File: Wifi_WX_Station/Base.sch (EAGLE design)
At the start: 75 parts, among them IC1 3.3v, J1 RJ45-8VERT, J6 M05X22X5FE, Q1 32.768Khz, U1 CP2104-GM, U2 25LC512, U3 PIC24FJ128GA008

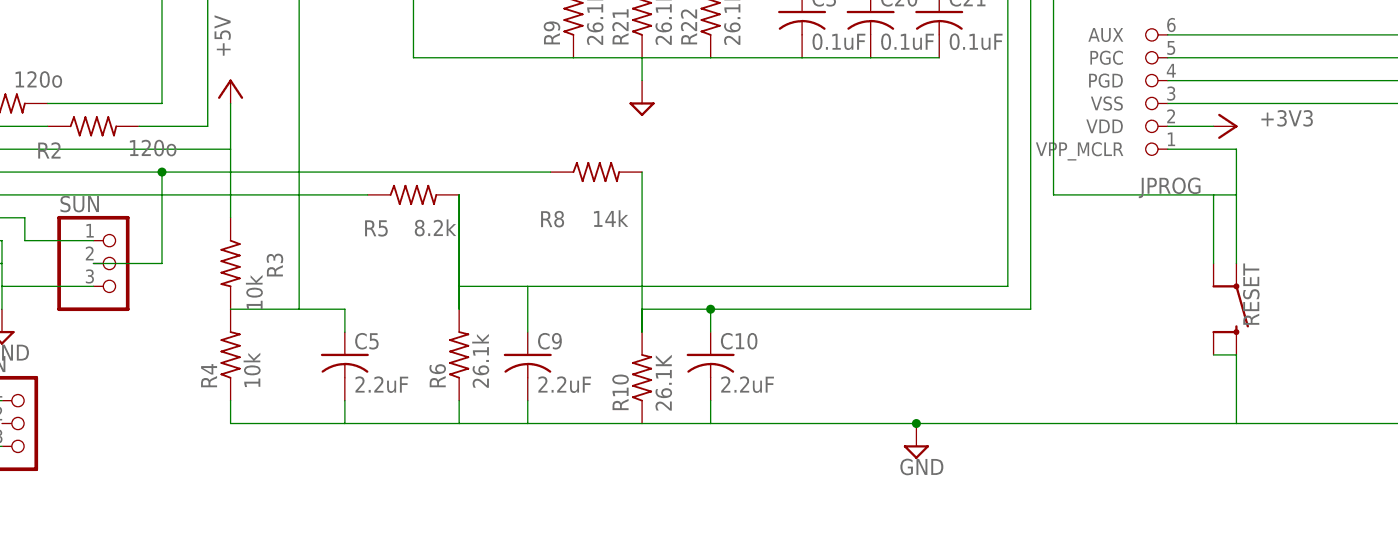
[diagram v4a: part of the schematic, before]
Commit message: 
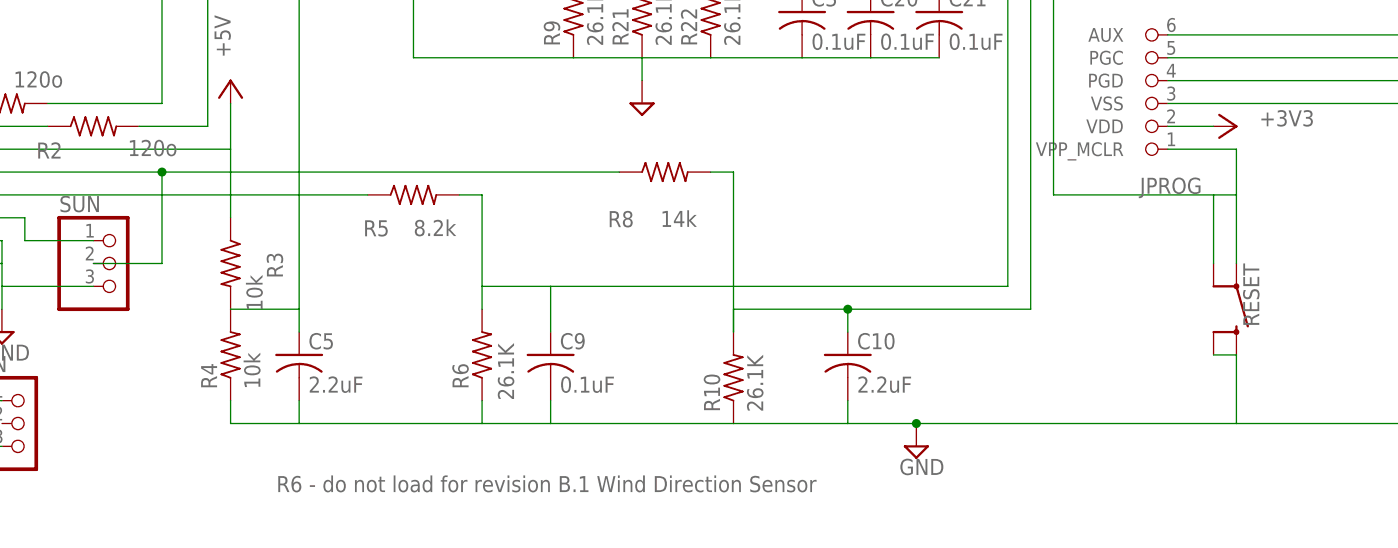
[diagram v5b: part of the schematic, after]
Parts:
- C9: value 2.2uF -> 0.1uF
- R6: value 26.1k -> 26.1K
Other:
- note added: "R6 - do not load for revision B.1 Wind Direction Sensor"
- moved on the sheet: C10, C5, C9, R10, R6, R8
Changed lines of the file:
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@@
 <part name="P+1" library="supply1" deviceset="+5V" device=""/>
 <part name="R5" library="rcl" deviceset="R-US_" device="R0603" value="8.2k"/>
-<part name="R6" library="rcl" deviceset="R-US_" device="R0603" value="26.1k"/>
-<part name="C9" library="rcl" deviceset="C-US" device="C0805" value="2.2uF"/>
+<part name="R6" library="rcl" deviceset="R-US_" device="R0603" value="26.1K"/>
+<part name="C9" library="rcl" deviceset="C-US" device="C0805" value="0.1uF"/>
 <part name="R13" library="rcl" deviceset="R-US_" device="R0603" value="2.2K"/>
 <part name="R3" library="rcl" deviceset="R-US_" device="R0603" value="10k"/>
@@
 <text x="-83.82" y="55.88" size="1.27" layer="95">PIC24FJ256GA108</text>
 <text x="43.18" y="78.74" size="1.778" layer="95">MRF24</text>
+<text x="-226.06" y="-40.64" size="1.778" layer="96">R6 - do not load for revision B.1 Wind Direction Sensor</text>
 </plain>
 <instances>
@@
 <attribute name="VALUE" x="-210.82" y="-12.192" size="1.778" layer="96"/>
 </instance>
-<instance part="R6" gate="G$1" x="-205.74" y="-25.4" rot="R90"/>
-<instance part="C9" gate="G$1" x="-198.12" y="-25.4"/>
+<instance part="R6" gate="G$1" x="-203.2" y="-25.4" smashed="yes" rot="R90">
+<attribute name="NAME" x="-204.6986" y="-29.21" size="1.778" layer="95" rot="R90"/>
+<attribute name="VALUE" x="-201.422" y="-24.13" size="1.778" layer="96" rot="R270"/>
+</instance>
+<instance part="C9" gate="G$1" x="-195.58" y="-25.4"/>
 <instance part="R13" gate="G$1" x="-157.48" y="106.68" smashed="yes" rot="R90">
 <attribute name="NAME" x="-158.9786" y="100.33" size="1.778" layer="95" rot="R90"/>
@@
 <attribute name="VALUE" x="-229.362" y="-16.51" size="1.778" layer="96" rot="R270"/>
 </instance>
-<instance part="C10" gate="G$1" x="-177.8" y="-25.4"/>
-<instance part="R8" gate="G$1" x="-190.5" y="-5.08" smashed="yes">
-<attribute name="NAME" x="-196.85" y="-11.2014" size="1.778" layer="95"/>
-<attribute name="VALUE" x="-191.008" y="-11.176" size="1.778" layer="96"/>
-</instance>
-<instance part="R10" gate="G$1" x="-185.42" y="-27.94" rot="R90"/>
+<instance part="C10" gate="G$1" x="-162.56" y="-25.4"/>
+<instance part="R8" gate="G$1" x="-182.88" y="-5.08" smashed="yes">
+<attribute name="NAME" x="-189.23" y="-11.2014" size="1.778" layer="95"/>
+<attribute name="VALUE" x="-183.388" y="-11.176" size="1.778" layer="96"/>
+</instance>
+<instance part="R10" gate="G$1" x="-175.26" y="-27.94" rot="R90"/>
 <instance part="R4" gate="G$1" x="-231.14" y="-25.4" rot="R90"/>
 <instance part="R15" gate="G$1" x="-152.4" y="106.68" smashed="yes" rot="R90">
@@
 <instance part="C16" gate="G$1" x="-187.96" y="111.76"/>
 <instance part="C18" gate="G$1" x="-175.26" y="111.76"/>
-<instance part="C5" gate="G$1" x="-218.44" y="-25.4"/>
+<instance part="C5" gate="G$1" x="-223.52" y="-25.4"/>
 <instance part="SUPPLY11" gate="GND" x="-264.16" y="-40.64"/>
 <instance part="P+3" gate="1" x="-264.16" y="-25.4" smashed="yes">
@@
 <pinref part="C9" gate="G$1" pin="2"/>
 <pinref part="R6" gate="G$1" pin="1"/>
-<wire x1="-205.74" y1="-30.48" x2="-205.74" y2="-33.02" width="0.1524" layer="91"/>
+<wire x1="-203.2" y1="-30.48" x2="-203.2" y2="-33.02" width="0.1524" layer="91"/>
 <pinref part="C10" gate="G$1" pin="2"/>
-<wire x1="-198.12" y1="-33.02" x2="-205.74" y2="-33.02" width="0.1524" layer="91"/>
-<wire x1="-198.12" y1="-30.48" x2="-198.12" y2="-33.02" width="0.1524" layer="91"/>
-<wire x1="-198.12" y1="-33.02" x2="-185.42" y2="-33.02" width="0.1524" layer="91"/>
-<wire x1="-185.42" y1="-33.02" x2="-177.8" y2="-33.02" width="0.1524" layer="91"/>
-<wire x1="-177.8" y1="-33.02" x2="-177.8" y2="-30.48" width="0.1524" layer="91"/>
+<wire x1="-195.58" y1="-33.02" x2="-203.2" y2="-33.02" width="0.1524" layer="91"/>
+<wire x1="-195.58" y1="-30.48" x2="-195.58" y2="-33.02" width="0.1524" layer="91"/>
+<wire x1="-195.58" y1="-33.02" x2="-175.26" y2="-33.02" width="0.1524" layer="91"/>
+<wire x1="-175.26" y1="-33.02" x2="-162.56" y2="-33.02" width="0.1524" layer="91"/>
+<wire x1="-162.56" y1="-33.02" x2="-162.56" y2="-30.48" width="0.1524" layer="91"/>
 <pinref part="R10" gate="G$1" pin="1"/>
 <pinref part="R4" gate="G$1" pin="1"/>
-<wire x1="-177.8" y1="-33.02" x2="-119.38" y2="-33.02" width="0.1524" layer="91"/>
+<wire x1="-162.56" y1="-33.02" x2="-119.38" y2="-33.02" width="0.1524" layer="91"/>
 <wire x1="-119.38" y1="-33.02" x2="-83.82" y2="-33.02" width="0.1524" layer="91"/>
 <wire x1="-231.14" y1="-30.48" x2="-231.14" y2="-33.02" width="0.1524" layer="91"/>
-<wire x1="-231.14" y1="-33.02" x2="-218.44" y2="-33.02" width="0.1524" layer="91"/>
+<wire x1="-231.14" y1="-33.02" x2="-223.52" y2="-33.02" width="0.1524" layer="91"/>
 <pinref part="C5" gate="G$1" pin="2"/>
-<wire x1="-218.44" y1="-33.02" x2="-205.74" y2="-33.02" width="0.1524" layer="91"/>
-<wire x1="-218.44" y1="-30.48" x2="-218.44" y2="-33.02" width="0.1524" layer="91"/>
+<wire x1="-223.52" y1="-33.02" x2="-203.2" y2="-33.02" width="0.1524" layer="91"/>
+<wire x1="-223.52" y1="-30.48" x2="-223.52" y2="-33.02" width="0.1524" layer="91"/>
 <pinref part="SV1" gate="G$1" pin="1"/>
 <pinref part="RESET" gate="G$1" pin="2"/>
@@
 <net name="WIND_ADC_IN" class="0">
 <segment>
-<wire x1="-144.78" y1="-17.78" x2="-198.12" y2="-17.78" width="0.1524" layer="91"/>
-<wire x1="-205.74" y1="-17.78" x2="-205.74" y2="-7.62" width="0.1524" layer="91"/>
+<wire x1="-144.78" y1="-17.78" x2="-195.58" y2="-17.78" width="0.1524" layer="91"/>
+<wire x1="-203.2" y1="-17.78" x2="-203.2" y2="-7.62" width="0.1524" layer="91"/>
+<wire x1="-203.2" y1="-7.62" x2="-205.74" y2="-7.62" width="0.1524" layer="91"/>
 <pinref part="R6" gate="G$1" pin="2"/>
 <pinref part="C9" gate="G$1" pin="1"/>
-<wire x1="-205.74" y1="-20.32" x2="-205.74" y2="-17.78" width="0.1524" layer="91"/>
-<wire x1="-205.74" y1="-17.78" x2="-198.12" y2="-17.78" width="0.1524" layer="91"/>
-<wire x1="-198.12" y1="-17.78" x2="-198.12" y2="-22.86" width="0.1524" layer="91"/>
+<wire x1="-203.2" y1="-20.32" x2="-203.2" y2="-17.78" width="0.1524" layer="91"/>
+<wire x1="-203.2" y1="-17.78" x2="-195.58" y2="-17.78" width="0.1524" layer="91"/>
+<wire x1="-195.58" y1="-17.78" x2="-195.58" y2="-22.86" width="0.1524" layer="91"/>
 <pinref part="R5" gate="G$1" pin="2"/>
 <pinref part="U3" gate="G$1" pin="C1IN-/AN4/CN6/RB4"/>
 <wire x1="-144.78" y1="-17.78" x2="-144.78" y2="35.56" width="0.1524" layer="91"/>
 <wire x1="-144.78" y1="35.56" x2="-134.62" y2="35.56" width="0.1524" layer="91"/>
-<wire x1="-205.74" y1="-7.62" x2="-205.74" y2="-20.32" width="0.1524" layer="91"/>
 </segment>
 </net>
@@
 <segment>
 <wire x1="-142.24" y1="33.02" x2="-142.24" y2="-20.32" width="0.1524" layer="91"/>
-<wire x1="-142.24" y1="-20.32" x2="-177.8" y2="-20.32" width="0.1524" layer="91"/>
+<wire x1="-142.24" y1="-20.32" x2="-162.56" y2="-20.32" width="0.1524" layer="91"/>
 <pinref part="R8" gate="G$1" pin="2"/>
 <pinref part="R10" gate="G$1" pin="2"/>
-<wire x1="-177.8" y1="-20.32" x2="-185.42" y2="-20.32" width="0.1524" layer="91"/>
-<wire x1="-185.42" y1="-20.32" x2="-185.42" y2="-22.86" width="0.1524" layer="91"/>
-<wire x1="-185.42" y1="-22.86" x2="-185.42" y2="-5.08" width="0.1524" layer="91"/>
+<wire x1="-162.56" y1="-20.32" x2="-175.26" y2="-20.32" width="0.1524" layer="91"/>
+<wire x1="-175.26" y1="-20.32" x2="-175.26" y2="-22.86" width="0.1524" layer="91"/>
+<wire x1="-175.26" y1="-22.86" x2="-175.26" y2="-5.08" width="0.1524" layer="91"/>
+<wire x1="-175.26" y1="-5.08" x2="-177.8" y2="-5.08" width="0.1524" layer="91"/>
 <pinref part="U3" gate="G$1" pin="C2IN+/AN3/CN5/RB3"/>
 <wire x1="-142.24" y1="33.02" x2="-134.62" y2="33.02" width="0.1524" layer="91"/>
 <pinref part="C10" gate="G$1" pin="1"/>
-<wire x1="-177.8" y1="-22.86" x2="-177.8" y2="-20.32" width="0.1524" layer="91"/>
-<junction x="-177.8" y="-20.32"/>
+<wire x1="-162.56" y1="-22.86" x2="-162.56" y2="-20.32" width="0.1524" layer="91"/>
+<junction x="-162.56" y="-20.32"/>
 </segment>
 </net>
@@
 <segment>
 <pinref part="R8" gate="G$1" pin="1"/>
-<wire x1="-195.58" y1="-5.08" x2="-238.76" y2="-5.08" width="0.1524" layer="91"/>
+<wire x1="-187.96" y1="-5.08" x2="-238.76" y2="-5.08" width="0.1524" layer="91"/>
 <label x="-281.94" y="-5.08" size="0.8128" layer="95" rot="R180" xref="yes"/>
 <wire x1="-238.76" y1="-5.08" x2="-264.16" y2="-5.08" width="0.1524" layer="91"/>
@@
 <segment>
 <wire x1="-223.52" y1="38.1" x2="-134.62" y2="38.1" width="0.1524" layer="91"/>
-<wire x1="-218.44" y1="-20.32" x2="-223.52" y2="-20.32" width="0.1524" layer="91"/>
 <wire x1="-223.52" y1="-20.32" x2="-223.52" y2="38.1" width="0.1524" layer="91"/>
 <pinref part="U3" gate="G$1" pin="C1IN+/AN5/CN7/RB5"/>
@@
 <pinref part="R3" gate="G$1" pin="2"/>
 <pinref part="C5" gate="G$1" pin="1"/>
-<wire x1="-218.44" y1="-22.86" x2="-218.44" y2="-20.32" width="0.1524" layer="91"/>
+<wire x1="-223.52" y1="-22.86" x2="-223.52" y2="-20.32" width="0.1524" layer="91"/>
 <wire x1="-223.52" y1="-20.32" x2="-231.14" y2="-20.32" width="0.1524" layer="91"/>
 </segment>

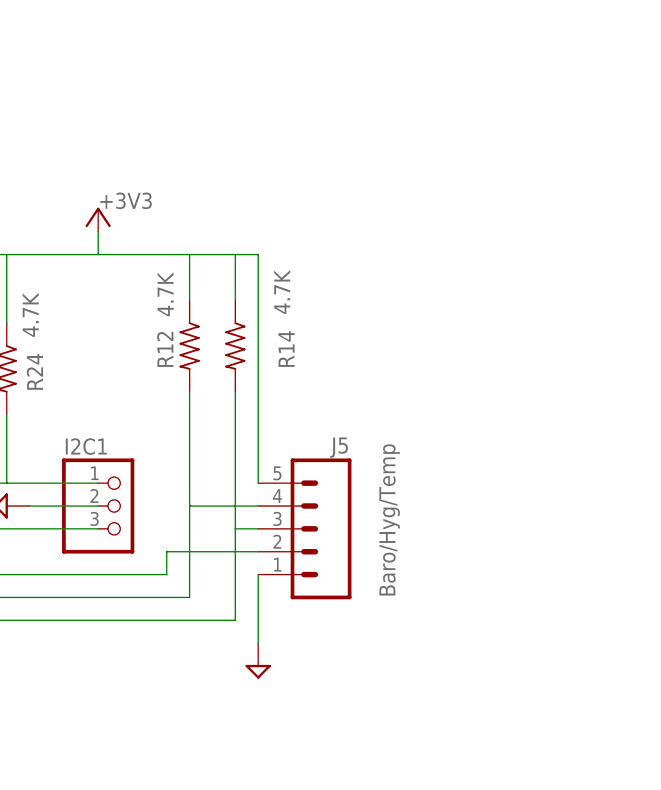
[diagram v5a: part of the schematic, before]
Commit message: Changed to RJ11 connector for Baro_temp_hyg  on base board -- Cleaned up some silk screen stuff Added new RJ11 based Baro_Temp_Hyg board layout
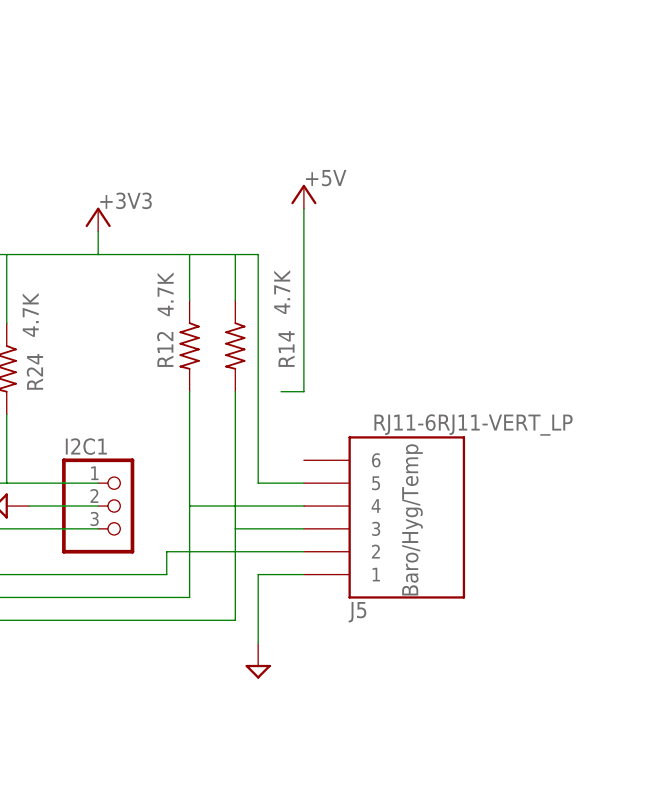
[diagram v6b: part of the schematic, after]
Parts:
- J5: value (none) -> RJ11-6RJ11-VERT_LP; device wifi_WX:M05MOLEX_KK -> wifi_WX:RJ11-6RJ11-VERT_LP
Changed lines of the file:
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@@
 <part name="C20" library="rcl" deviceset="C-US" device="C0805" value="0.1uF"/>
 <part name="C21" library="rcl" deviceset="C-US" device="C0805" value="0.1uF"/>
-<part name="J5" library="wifi_WX" deviceset="M05" device="MOLEX_KK"/>
 <part name="SUPPLY13" library="supply2" deviceset="GND" device=""/>
 <part name="R23" library="rcl" deviceset="R-US_" device="R0603" value="4.7K"/>
@@
 <part name="P+4" library="supply1" deviceset="+5V" device=""/>
 <part name="D2" library="diode" deviceset="MBR0520LT" device=""/>
+<part name="P+5" library="supply1" deviceset="+5V" device=""/>
+<part name="J5" library="wifi_WX" deviceset="RJ11-6" device="RJ11-VERT_LP"/>
 </parts>
 <sheets>
 <sheet>
 <plain>
-<text x="124.46" y="40.64" size="1.778" layer="95" rot="R90">Baro/Hyg/Temp</text>
+<text x="127" y="40.64" size="1.778" layer="95" rot="R90">Baro/Hyg/Temp</text>
 <text x="-83.82" y="55.88" size="1.27" layer="95">PIC24FJ256GA108</text>
 <text x="43.18" y="78.74" size="1.778" layer="95">MRF24</text>
@@
 <instance part="C20" gate="G$1" x="-160.02" y="12.7"/>
 <instance part="C21" gate="G$1" x="-152.4" y="12.7"/>
-<instance part="J5" gate="G$1" x="116.84" y="48.26" rot="MR0"/>
 <instance part="SUPPLY13" gate="GND" x="81.28" y="50.8" smashed="yes" rot="R270"/>
 <instance part="R23" gate="G$1" x="76.2" y="66.04" smashed="yes" rot="R270">
@@
 </instance>
 <instance part="D2" gate="G$1" x="-233.68" y="33.02" rot="R270"/>
+<instance part="P+5" gate="1" x="114.3" y="86.36" smashed="yes">
+<attribute name="VALUE" x="114.3" y="86.36" size="1.778" layer="96"/>
+</instance>
+<instance part="J5" gate="G$1" x="124.46" y="53.34" rot="MR180"/>
 </instances>
 <busses>
@@
 <segment>
 <pinref part="SUPPLY12" gate="GND" pin="GND"/>
+<wire x1="109.22" y1="43.18" x2="109.22" y2="35.56" width="0.1524" layer="91"/>
+<wire x1="109.22" y1="43.18" x2="114.3" y2="43.18" width="0.1524" layer="91"/>
 <pinref part="J5" gate="G$1" pin="1"/>
-<wire x1="109.22" y1="43.18" x2="109.22" y2="35.56" width="0.1524" layer="91"/>
 </segment>
 <segment>
@@
 <wire x1="91.44" y1="78.74" x2="101.6" y2="78.74" width="0.1524" layer="91"/>
 <wire x1="106.68" y1="78.74" x2="101.6" y2="78.74" width="0.1524" layer="91"/>
-<pinref part="J5" gate="G$1" pin="5"/>
 <wire x1="109.22" y1="78.74" x2="109.22" y2="53.34" width="0.1524" layer="91"/>
 <wire x1="106.68" y1="78.74" x2="109.22" y2="78.74" width="0.1524" layer="91"/>
@@
 <wire x1="81.28" y1="78.74" x2="91.44" y2="78.74" width="0.1524" layer="91"/>
 <wire x1="81.28" y1="71.12" x2="81.28" y2="78.74" width="0.1524" layer="91"/>
+<wire x1="109.22" y1="53.34" x2="114.3" y2="53.34" width="0.1524" layer="91"/>
+<pinref part="J5" gate="G$1" pin="5"/>
 </segment>
 </net>
@@
 <wire x1="-12.7" y1="40.64" x2="101.6" y2="40.64" width="0.1524" layer="91"/>
 <wire x1="101.6" y1="40.64" x2="101.6" y2="50.8" width="0.1524" layer="91"/>
-<wire x1="101.6" y1="50.8" x2="109.22" y2="50.8" width="0.1524" layer="91"/>
+<wire x1="101.6" y1="50.8" x2="114.3" y2="50.8" width="0.1524" layer="91"/>
 <pinref part="U3" gate="G$1" pin="SCL1/RG2"/>
 <label x="71.12" y="40.64" size="1.27" layer="95" rot="R180" xref="yes"/>
@@
 <wire x1="-12.7" y1="38.1" x2="106.68" y2="38.1" width="0.1524" layer="91"/>
 <wire x1="106.68" y1="38.1" x2="106.68" y2="48.26" width="0.1524" layer="91"/>
-<wire x1="106.68" y1="48.26" x2="109.22" y2="48.26" width="0.1524" layer="91"/>
 <pinref part="U3" gate="G$1" pin="SDA1/RG3"/>
 <label x="71.12" y="38.1" size="1.27" layer="95" rot="R180" xref="yes"/>
 <pinref part="R14" gate="G$1" pin="2"/>
 <wire x1="106.68" y1="63.5" x2="106.68" y2="48.26" width="0.1524" layer="91"/>
+<wire x1="106.68" y1="48.26" x2="114.3" y2="48.26" width="0.1524" layer="91"/>
 <pinref part="J5" gate="G$1" pin="3"/>
 </segment>
@@
 <net name="BARO_CS" class="0">
 <segment>
-<wire x1="109.22" y1="45.72" x2="99.06" y2="45.72" width="0.1524" layer="91"/>
+<wire x1="114.3" y1="45.72" x2="99.06" y2="45.72" width="0.1524" layer="91"/>
 <wire x1="99.06" y1="45.72" x2="99.06" y2="43.18" width="0.1524" layer="91"/>
 <wire x1="99.06" y1="43.18" x2="15.24" y2="43.18" width="0.1524" layer="91"/>
@@
 <wire x1="15.24" y1="58.42" x2="15.24" y2="43.18" width="0.1524" layer="91"/>
 <pinref part="U3" gate="G$1" pin="IC1/RTCC/RD8"/>
+<label x="71.12" y="43.18" size="1.27" layer="95" rot="R180" xref="yes"/>
 <pinref part="J5" gate="G$1" pin="2"/>
-<label x="71.12" y="43.18" size="1.27" layer="95" rot="R180" xref="yes"/>
 </segment>
 </net>
@@
 <pinref part="P+4" gate="1" pin="+5V"/>
 </segment>
-</net>
+<segment>
+<pinref part="P+5" gate="1" pin="+5V"/>
+<wire x1="114.3" y1="83.82" x2="114.3" y2="63.5" width="0.1524" layer="91"/>
+<wire x1="114.3" y1="63.5" x2="111.76" y2="63.5" width="0.1524" layer="91"/>
+</segment>
+</net>

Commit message: added SILabs Hygrometer board Added frames to the schematics
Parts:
- C7: value 330uF/6V -> 220uF/6.3V
- R19, R20, R7: value 14k -> 100K
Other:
- note added: "*"
- note added: "B.2"
- note added: "R7,R19,R20 Use 100K for 15V ADC input range."
- note added: "R7,R19,R20 use 14Ko for 5V ADC input range"
- note added: "WunderWxStation"
- moved on the sheet: +5V, FAN, USB

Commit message: Added multiple new boards - H-pwrdist- Insp_Wind_enc, 5040 etc..
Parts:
- J5: value RJ11-6RJ11-VERT_LP -> RJ11-6VERT_LP; device wifi_WX:RJ11-6RJ11-VERT_LP -> wifi_WX:RJ11-6VERT_LP
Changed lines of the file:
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@@
 <part name="P+4" library="supply1" deviceset="+5V" device=""/>
 <part name="D2" library="diode" deviceset="MBR0520LT" device=""/>
-<part name="J5" library="wifi_WX" deviceset="RJ11-6" device="RJ11-VERT_LP"/>
+<part name="J5" library="wifi_WX" deviceset="RJ11-6" device="VERT_LP"/>
 <part name="U$1" library="1AA_Stofer" deviceset="11X17" device=""/>
 <part name="U$2" library="1AA_Stofer" deviceset="10.5X18" device=""/>
